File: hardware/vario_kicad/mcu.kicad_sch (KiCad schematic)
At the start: 22 parts, among them U5 STM32L072CBTx, Y1 Crystal, Y2 Crystal_GND24

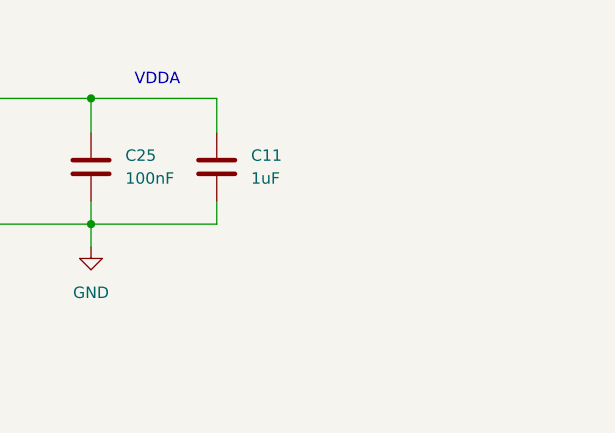
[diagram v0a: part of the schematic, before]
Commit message: add decoupling capacitor for vdd_usb
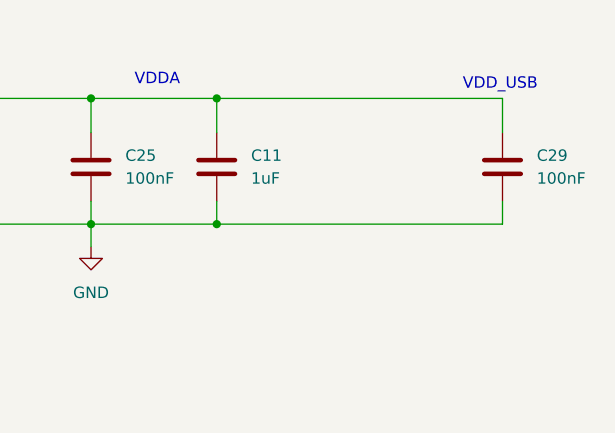
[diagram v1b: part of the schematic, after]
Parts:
- added C29: 100nF, Capacitor_SMD:C_0603_1608Metric, symbol Device:C
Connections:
- net GND: now also C29.2
- net VCC: now also C29.1
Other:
- note added: "VDD_USB"
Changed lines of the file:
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@@
 	(paper "A3")
 	(junction
+		(at 311.15 93.98)
+		(diameter 0)
+		(color 0 0 0 0)
+	)
+	(junction
 		(at 162.56 93.98)
 		(diameter 0)
@@
 	)
 	(junction
+		(at 311.15 107.95)
+		(diameter 0)
+		(color 0 0 0 0)
+	)
+	(junction
 		(at 240.03 107.95)
 		(diameter 0)
@@
 	(wire
 		(pts
+			(xy 311.15 107.95) (xy 342.9 107.95)
+		)
+		(stroke
+			(width 0)
+			(type default)
+		)
+	)
+	(wire
+		(pts
 			(xy 45.72 214.63) (xy 45.72 218.44)
 		)
@@
 	(wire
 		(pts
+			(xy 342.9 93.98) (xy 342.9 97.79)
+		)
+		(stroke
+			(width 0)
+			(type default)
+		)
+	)
+	(wire
+		(pts
 			(xy 123.19 101.6) (xy 123.19 104.14)
 		)
@@
 	(wire
 		(pts
+			(xy 342.9 107.95) (xy 342.9 105.41)
+		)
+		(stroke
+			(width 0)
+			(type default)
+		)
+	)
+	(wire
+		(pts
 			(xy 77.47 153.67) (xy 77.47 156.21)
 		)
@@
 		)
 	)
+	(wire
+		(pts
+			(xy 311.15 93.98) (xy 342.9 93.98)
+		)
+		(stroke
+			(width 0)
+			(type default)
+		)
+	)
 	(rectangle
 		(start 41.91 139.192)
@@
 		)
 	)
+	(text "VDD_USB"
+		(exclude_from_sim no)
+		(at 342.646 92.456 0)
+		(effects
+			(font
+				(size 1.27 1.27)
+			)
+		)
+	)
 	(text "LSE"
 		(exclude_from_sim no)
@@
 					(unit 1)
 				)
+			)
+		)
+	)
+	(symbol
+		(lib_id "Device:C")
+		(at 342.9 101.6 0)
+		(unit 1)
+		(exclude_from_sim no)
+		(in_bom yes)
+		(on_board yes)
+		(dnp no)
+		(fields_autoplaced yes)
+		(property "Reference" "C29"
+			(at 346.71 100.3299 0)
+			(effects
+				(font
+					(size 1.27 1.27)
+				)
+				(justify left)
+			)
+		)
+		(property "Value" "100nF"
+			(at 346.71 102.8699 0)
+			(effects
+				(font
+					(size 1.27 1.27)
+				)
+				(justify left)
+			)
+		)
+		(property "Footprint" "Capacitor_SMD:C_0603_1608Metric"
+			(at 343.8652 105.41 0)
+			(effects
+				(font
+					(size 1.27 1.27)
+				)
+				(hide yes)
+			)
+		)
+		(property "Datasheet" "~"
+			(at 342.9 101.6 0)
+			(effects
+				(font
+					(size 1.27 1.27)
+				)
+				(hide yes)
+			)
+		)
+		(property "Description" "Unpolarized capacitor"
+			(at 342.9 101.6 0)
+			(effects
+				(font
+					(size 1.27 1.27)
+				)
+				(hide yes)
+			)
+		)
+		(property "Sim.Pins" ""
+			(at 342.9 101.6 0)
+			(effects
+				(font
+					(size 1.27 1.27)
+				)
+				(hide yes)
+			)
+		)
+		(pin "2"
+		)
+		(pin "1"
+		)
+		(instances
+			(project "vario_kicad"
+				(path "/50389aff-b244-451e-8e3a-c5addd2215e1/dd2cba4c-5ed6-4588-88fb-827c05b79647"
+					(reference "C29")
+					(unit 1)
+				)

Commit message: add missing footprints
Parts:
- R30: footprint (none) -> Resistor_SMD:R_0402_1005Metric
- TP4: footprint (none) -> TestPoint:TestPoint_Pad_D1.0mm
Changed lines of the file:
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@@
 			)
 		)
-		(property "Footprint" ""
+		(property "Footprint" "Resistor_SMD:R_0402_1005Metric"
 			(at 109.22 230.378 90)
 			(effects
@@
 			)
 		)
-		(property "Footprint" ""
+		(property "Footprint" "TestPoint:TestPoint_Pad_D1.0mm"
 			(at 90.17 121.92 0)
 			(effects

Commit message: layout close to done
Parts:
- removed TP11, TP12: TestPoint, TestPoint:TestPoint_Pad_D1.0mm, symbol Connector:TestPoint
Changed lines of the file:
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@@
-	)
-	(junction
-		(at 203.2 134.62)
-		(diameter 0)
-		(color 0 0 0 0)
 	)
 	(junction
@@
 	)
 	(junction
-		(at 203.2 132.08)
-		(diameter 0)
-		(color 0 0 0 0)
-	)
-	(junction
 		(at 252.73 93.98)
 		(diameter 0)
@@
 	(wire
 		(pts
-			(xy 175.26 134.62) (xy 203.2 134.62)
-		)
-		(stroke
-			(width 0)
-			(type default)
-		)
-	)
-	(wire
-		(pts
 			(xy 128.27 134.62) (xy 139.7 134.62)
 		)
@@
 	(wire
 		(pts
-			(xy 203.2 134.62) (xy 207.01 134.62)
+			(xy 175.26 134.62) (xy 207.01 134.62)
 		)
 		(stroke
@@
 	(wire
 		(pts
-			(xy 203.2 132.08) (xy 207.01 132.08)
+			(xy 175.26 132.08) (xy 207.01 132.08)
 		)
 		(stroke
@@
 		(pts
 			(xy 265.43 93.98) (xy 297.18 93.98)
-		)
-		(stroke
-			(width 0)
-			(type default)
-		)
-	)
-	(wire
-		(pts
-			(xy 175.26 132.08) (xy 203.2 132.08)
 		)
 		(stroke
@@
 	)
 	(symbol
-		(lib_id "Connector:TestPoint")
-		(at 203.2 134.62 180)
-		(unit 1)
-		(exclude_from_sim no)
-		(in_bom yes)
-		(on_board yes)
-		(dnp no)
-		(property "Reference" "TP12"
-			(at 204.216 138.684 0)
-			(effects
-				(font
-					(size 1.27 1.27)
-				)
-				(justify right)
-			)
-		)
-		(property "Value" "TestPoint"
-			(at 205.74 139.1919 0)
-			(effects
-				(font
-					(size 1.27 1.27)
-				)
-				(justify right)
-				(hide yes)
-			)
-		)
-		(property "Footprint" "TestPoint:TestPoint_Pad_D1.0mm"
-			(at 198.12 134.62 0)
-			(effects
-				(font
-					(size 1.27 1.27)
-				)
-				(hide yes)
-			)
-		)
-		(property "Datasheet" "~"
-			(at 198.12 134.62 0)
-			(effects
-				(font
-					(size 1.27 1.27)
-				)
-				(hide yes)
-			)
-		)
-		(property "Description" "test point"
-			(at 203.2 134.62 0)
-			(effects
-				(font
-					(size 1.27 1.27)
-				)
-				(hide yes)
-			)
-		)
-		(property "Sim.Pins" ""
-			(at 203.2 134.62 0)
-			(effects
-				(font
-					(size 1.27 1.27)
-				)
-				(hide yes)
-			)
-		)
-		(pin "1"
-		)
-		(instances
-			(project "vario_kicad"
-				(path "/50389aff-b244-451e-8e3a-c5addd2215e1/dd2cba4c-5ed6-4588-88fb-827c05b79647"
-					(reference "TP12")
-					(unit 1)
-				)
-			)
-		)
-	)
-	(symbol
 		(lib_id "MCU_ST_STM32L0:STM32L072CBTx")
 		(at 157.48 137.16 0)
@@
 					(unit 1)
 				)
-			)
-		)
-	)
-	(symbol
-		(lib_id "Connector:TestPoint")
-		(at 203.2 132.08 0)
-		(unit 1)
-		(exclude_from_sim no)
-		(in_bom yes)
-		(on_board yes)
-		(dnp no)
-		(property "Reference" "TP11"
-			(at 203.962 127.762 0)
-			(effects
-				(font
-					(size 1.27 1.27)
-				)
-				(justify left)
-			)
-		)
-		(property "Value" "TestPoint"
-			(at 205.74 130.0479 0)
-			(effects
-				(font
-					(size 1.27 1.27)
-				)
-				(justify left)
-				(hide yes)
-			)
-		)
-		(property "Footprint" "TestPoint:TestPoint_Pad_D1.0mm"
-			(at 208.28 132.08 0)
-			(effects
-				(font
-					(size 1.27 1.27)
-				)
-				(hide yes)
-			)
-		)
-		(property "Datasheet" "~"
-			(at 208.28 132.08 0)
-			(effects
-				(font
-					(size 1.27 1.27)
-				)
-				(hide yes)
-			)
-		)
-		(property "Description" "test point"
-			(at 203.2 132.08 0)
-			(effects
-				(font
-					(size 1.27 1.27)
-				)
-				(hide yes)
-			)
-		)
-		(property "Sim.Pins" ""
-			(at 203.2 132.08 0)
-			(effects
-				(font
-					(size 1.27 1.27)
-				)
-				(hide yes)
-			)
-		)
-		(pin "1"
-		)
-		(instances
-			(project "vario_kicad"
-				(path "/50389aff-b244-451e-8e3a-c5addd2215e1/dd2cba4c-5ed6-4588-88fb-827c05b79647"
-					(reference "TP11")
-					(unit 1)
-				)

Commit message: remove unnecessary jumper
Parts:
- removed JP1: SolderJumper_2_Bridged, Jumper:SolderJumper-2_P1.3mm_Open_TrianglePad1.0x1.5mm, symbol Jumper:SolderJumper_2_Bridged
- R30: now fitted
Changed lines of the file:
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@@
-	)
-	(junction
-		(at 97.79 218.44)
-		(diameter 0)
-		(color 0 0 0 0)
 	)
 	(junction
@@
 	)
 	(junction
-		(at 120.65 218.44)
-		(diameter 0)
-		(color 0 0 0 0)
-	)
-	(junction
 		(at 157.48 93.98)
 		(diameter 0)
@@
 	(wire
 		(pts
-			(xy 113.03 208.28) (xy 120.65 208.28)
-		)
-		(stroke
-			(width 0)
-			(type default)
-		)
-	)
-	(wire
-		(pts
 			(xy 58.42 171.45) (xy 68.58 171.45)
 		)
@@
 	(wire
 		(pts
-			(xy 120.65 208.28) (xy 120.65 218.44)
-		)
-		(stroke
-			(width 0)
-			(type default)
-		)
-	)
-	(wire
-		(pts
 			(xy 64.77 218.44) (xy 45.72 218.44)
 		)
@@
 	(wire
 		(pts
-			(xy 97.79 218.44) (xy 97.79 208.28)
-		)
-		(stroke
-			(width 0)
-			(type default)
-		)
-	)
-	(wire
-		(pts
 			(xy 240.03 105.41) (xy 240.03 107.95)
 		)
@@
 	(wire
 		(pts
-			(xy 120.65 218.44) (xy 120.65 228.6)
-		)
-		(stroke
-			(width 0)
-			(type default)
-		)
-	)
-	(wire
-		(pts
 			(xy 297.18 93.98) (xy 311.15 93.98)
 		)
@@
 	(wire
 		(pts
-			(xy 97.79 208.28) (xy 105.41 208.28)
-		)
-		(stroke
-			(width 0)
-			(type default)
-		)
-	)
-	(wire
-		(pts
 			(xy 175.26 104.14) (xy 182.88 104.14)
 		)
@@
 	(wire
 		(pts
-			(xy 97.79 228.6) (xy 105.41 228.6)
-		)
-		(stroke
-			(width 0)
-			(type default)
-		)
-	)
-	(wire
-		(pts
 			(xy 76.2 109.22) (xy 113.03 109.22)
 		)
@@
 	(wire
 		(pts
-			(xy 86.36 218.44) (xy 97.79 218.44)
+			(xy 86.36 218.44) (xy 96.52 218.44)
 		)
 		(stroke
@@
 	(wire
 		(pts
-			(xy 120.65 218.44) (xy 132.08 218.44)
+			(xy 104.14 218.44) (xy 116.84 218.44)
 		)
 		(stroke
@@
 		(pts
 			(xy 157.48 179.07) (xy 154.94 179.07)
-		)
-		(stroke
-			(width 0)
-			(type default)
-		)
-	)
-	(wire
-		(pts
-			(xy 97.79 218.44) (xy 97.79 228.6)
-		)
-		(stroke
-			(width 0)
-			(type default)
-		)
-	)
-	(wire
-		(pts
-			(xy 120.65 228.6) (xy 113.03 228.6)
 		)
 		(stroke
@@
 	(rectangle
 		(start 35.306 197.866)
-		(end 147.828 251.46)
+		(end 130.81 251.46)
 		(stroke
 			(width 0)
@@
 	)
 	(label "OSC_OUT"
-		(at 132.08 218.44 0)
+		(at 116.84 218.44 0)
 		(effects
 			(font
@@
 	(symbol
 		(lib_id "Device:R")
-		(at 109.22 228.6 90)
+		(at 100.33 218.44 90)
 		(unit 1)
 		(exclude_from_sim no)
 		(in_bom yes)
 		(on_board yes)
-		(dnp yes)
+		(dnp no)
 		(fields_autoplaced yes)
 		(property "Reference" "R30"
-			(at 109.22 222.25 90)
+			(at 100.33 212.09 90)
 			(effects
 				(font
@@
 		)
 		(property "Value" "0R"
-			(at 109.22 224.79 90)
+			(at 100.33 214.63 90)
 			(effects
 				(font
@@
 		)
 		(property "Footprint" "Resistor_SMD:R_0402_1005Metric"
-			(at 109.22 230.378 90)
+			(at 100.33 220.218 90)
 			(effects
 				(font
@@
 		)
 		(property "Datasheet" "~"
-			(at 109.22 228.6 0)
+			(at 100.33 218.44 0)
 			(effects
 				(font
@@
 		)
 		(property "Description" "Resistor"
-			(at 109.22 228.6 0)
+			(at 100.33 218.44 0)
 			(effects
 				(font
@@
 					(unit 1)
 				)
-			)
-		)
-	)
-	(symbol
-		(lib_id "Jumper:SolderJumper_2_Bridged")
-		(at 109.22 208.28 0)
-		(unit 1)
-		(exclude_from_sim yes)
-		(in_bom no)
-		(on_board yes)
-		(dnp no)
-		(fields_autoplaced yes)
-		(property "Reference" "JP1"
-			(at 109.22 201.93 0)
-			(effects
-				(font
-					(size 1.27 1.27)
-				)
-			)
-		)
-		(property "Value" "SolderJumper_2_Bridged"
-			(at 109.22 204.47 0)
-			(effects
-				(font
-					(size 1.27 1.27)
-				)
-			)
-		)
-		(property "Footprint" "Jumper:SolderJumper-2_P1.3mm_Open_TrianglePad1.0x1.5mm"
-			(at 109.22 208.28 0)
-			(effects
-				(font
-					(size 1.27 1.27)
-				)
-				(hide yes)
-			)
-		)
-		(property "Datasheet" "~"
-			(at 109.22 208.28 0)
-			(effects
-				(font
-					(size 1.27 1.27)
-				)
-				(hide yes)
-			)
-		)
-		(property "Description" "Solder Jumper, 2-pole, closed/bridged"
-			(at 109.22 208.28 0)
-			(effects
-				(font
-					(size 1.27 1.27)
-				)
-				(hide yes)
-			)
-		)
-		(pin "1"
-		)
-		(pin "2"
-		)
-		(instances
-			(project ""
-				(path "/50389aff-b244-451e-8e3a-c5addd2215e1/dd2cba4c-5ed6-4588-88fb-827c05b79647"
-					(reference "JP1")
-					(unit 1)
-				)

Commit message: use 0402 instead of 0603 for almost all caps
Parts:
- C11, C12, C21, C22, C23, C24, C25, C29: footprint Capacitor_SMD:C_0603_1608Metric -> Capacitor_SMD:C_0402_1005Metric
- C4: footprint Capacitor_SMD:C_0603_1608Metric -> Capacitor_SMD:C_0603_1608Metric_Pad1.08x0.95mm_HandSolder
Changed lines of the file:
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@@
 			)
 		)
-		(property "Footprint" "Capacitor_SMD:C_0603_1608Metric"
+		(property "Footprint" "Capacitor_SMD:C_0402_1005Metric"
 			(at 298.1452 105.41 0)
 			(effects
@@
 			)
 		)
-		(property "Footprint" "Capacitor_SMD:C_0603_1608Metric"
+		(property "Footprint" "Capacitor_SMD:C_0402_1005Metric"
 			(at 77.1652 120.65 0)
 			(effects
@@
 			)
 		)
-		(property "Footprint" "Capacitor_SMD:C_0603_1608Metric"
+		(property "Footprint" "Capacitor_SMD:C_0402_1005Metric"
 			(at 266.3952 105.41 0)
 			(effects
@@
 			)
 		)
-		(property "Footprint" "Capacitor_SMD:C_0603_1608Metric"
+		(property "Footprint" "Capacitor_SMD:C_0603_1608Metric_Pad1.08x0.95mm_HandSolder"
 			(at 220.6752 105.41 0)
 			(effects
@@
 			)
 		)
-		(property "Footprint" "Capacitor_SMD:C_0603_1608Metric"
+		(property "Footprint" "Capacitor_SMD:C_0402_1005Metric"
 			(at 45.4152 114.3 0)
 			(effects
@@
 			)
 		)
-		(property "Footprint" "Capacitor_SMD:C_0603_1608Metric"
+		(property "Footprint" "Capacitor_SMD:C_0402_1005Metric"
 			(at 253.6952 105.41 0)
 			(effects
@@
 			)
 		)
-		(property "Footprint" "Capacitor_SMD:C_0603_1608Metric"
+		(property "Footprint" "Capacitor_SMD:C_0402_1005Metric"
 			(at 240.9952 105.41 0)
 			(effects
@@
 			)
 		)
-		(property "Footprint" "Capacitor_SMD:C_0603_1608Metric"
+		(property "Footprint" "Capacitor_SMD:C_0402_1005Metric"
 			(at 312.1152 105.41 0)
 			(effects
@@
 			)
 		)
-		(property "Footprint" "Capacitor_SMD:C_0603_1608Metric"
+		(property "Footprint" "Capacitor_SMD:C_0402_1005Metric"
 			(at 343.8652 105.41 0)
 			(effects

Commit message: layout close to finished
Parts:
- Y2: footprint Crystal:Crystal_SMD_3225-4Pin_3.2x2.5mm_HandSoldering -> Crystal:Crystal_SMD_3225-4Pin_3.2x2.5mm
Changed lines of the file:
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@@
 			)
 		)
-		(property "Footprint" "Crystal:Crystal_SMD_3225-4Pin_3.2x2.5mm_HandSoldering"
+		(property "Footprint" "Crystal:Crystal_SMD_3225-4Pin_3.2x2.5mm"
 			(at 68.58 218.44 0)
 			(effects

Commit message: layout&routing close to done
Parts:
- added C30: 100nF, Capacitor_SMD:C_0402_1005Metric, symbol Device:C
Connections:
- net ADC_IN3: now also C30.1
- net GND: now also C30.2
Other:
- note added: "noise decoupling cap"
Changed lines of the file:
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@@
+	)
+	(junction
+		(at 234.95 115.57)
+		(diameter 0)
+		(color 0 0 0 0)
 	)
 	(junction
@@
 	(wire
 		(pts
-			(xy 175.26 111.76) (xy 182.88 111.76)
+			(xy 234.95 115.57) (xy 243.84 115.57)
 		)
 		(stroke
@@
 	(wire
 		(pts
+			(xy 234.95 115.57) (xy 234.95 111.76)
+		)
+		(stroke
+			(width 0)
+			(type default)
+		)
+	)
+	(wire
+		(pts
 			(xy 113.03 109.22) (xy 139.7 109.22)
 		)
@@
 	(wire
 		(pts
+			(xy 234.95 111.76) (xy 175.26 111.76)
+		)
+		(stroke
+			(width 0)
+			(type default)
+		)
+	)
+	(wire
+		(pts
 			(xy 157.48 179.07) (xy 157.48 181.61)
 		)
@@
 	(wire
 		(pts
+			(xy 234.95 127) (xy 234.95 130.81)
+		)
+		(stroke
+			(width 0)
+			(type default)
+		)
+	)
+	(wire
+		(pts
 			(xy 45.72 237.49) (xy 68.58 237.49)
 		)
@@
 		(pts
 			(xy 311.15 93.98) (xy 342.9 93.98)
+		)
+		(stroke
+			(width 0)
+			(type default)
+		)
+	)
+	(wire
+		(pts
+			(xy 234.95 115.57) (xy 234.95 119.38)
 		)
 		(stroke
@@
 		)
 	)
+	(text "noise decoupling cap\n"
+		(exclude_from_sim no)
+		(at 243.078 127.762 0)
+		(effects
+			(font
+				(size 0.762 0.762)
+			)
+		)
+	)
 	(text "MCU"
 		(exclude_from_sim no)
@@
 	(hierarchical_label "ADC_IN3"
 		(shape input)
-		(at 182.88 111.76 0)
+		(at 243.84 115.57 0)
 		(effects
 			(font
@@
 	)
 	(symbol
+		(lib_id "power:GND")
+		(at 234.95 130.81 0)
+		(unit 1)
+		(exclude_from_sim no)
+		(in_bom yes)
+		(on_board yes)
+		(dnp no)
+		(fields_autoplaced yes)
+		(property "Reference" "#PWR39"
+			(at 234.95 137.16 0)
+			(effects
+				(font
+					(size 1.27 1.27)
+				)
+				(hide yes)
+			)
+		)
+		(property "Value" "GND"
+			(at 234.95 135.89 0)
+			(effects
+				(font
+					(size 1.27 1.27)
+				)
+			)
+		)
+		(property "Footprint" ""
+			(at 234.95 130.81 0)
+			(effects
+				(font
+					(size 1.27 1.27)
+				)
+				(hide yes)
+			)
+		)
+		(property "Datasheet" ""
+			(at 234.95 130.81 0)
+			(effects
+				(font
+					(size 1.27 1.27)
+				)
+				(hide yes)
+			)
+		)
+		(property "Description" "Power symbol creates a global label with name \"GND\" , ground"
+			(at 234.95 130.81 0)
+			(effects
+				(font
+					(size 1.27 1.27)
+				)
+				(hide yes)
+			)
+		)
+		(pin "1"
+		)
+		(instances
+			(project ""
+				(path "/50389aff-b244-451e-8e3a-c5addd2215e1/dd2cba4c-5ed6-4588-88fb-827c05b79647"
+					(reference "#PWR39")
+					(unit 1)
+				)
+			)
+		)
+	)
+	(symbol
 		(lib_id "Device:C")
 		(at 76.2 116.84 0)
@@
 					(unit 1)
 				)
+			)
+		)
+	)
+	(symbol
+		(lib_id "Device:C")
+		(at 234.95 123.19 0)
+		(unit 1)
+		(exclude_from_sim no)
+		(in_bom yes)
+		(on_board yes)
+		(dnp no)
+		(property "Reference" "C30"
+			(at 238.76 121.9199 0)
+			(effects
+				(font
+					(size 1.27 1.27)
+				)
+				(justify left)
+			)
+		)
+		(property "Value" "100nF"
+			(at 238.76 124.4599 0)
+			(effects
+				(font
+					(size 1.27 1.27)
+				)
+				(justify left)
+			)
+		)
+		(property "Footprint" "Capacitor_SMD:C_0402_1005Metric"
+			(at 235.9152 127 0)
+			(effects
+				(font
+					(size 1.27 1.27)
+				)
+				(hide yes)
+			)
+		)
+		(property "Datasheet" "~"
+			(at 234.95 123.19 0)
+			(effects
+				(font
+					(size 1.27 1.27)
+				)
+				(hide yes)
+			)
+		)
+		(property "Description" "Unpolarized capacitor"
+			(at 234.95 123.19 0)
+			(effects
+				(font
+					(size 1.27 1.27)
+				)
+				(hide yes)
+			)
+		)
+		(property "Sim.Pins" ""
+			(at 234.95 123.19 0)
+			(effects
+				(font
+					(size 1.27 1.27)
+				)
+				(hide yes)
+			)
+		)
+		(pin "2"
+		)
+		(pin "1"
+		)
+		(instances
+			(project "vario_kicad"
+				(path "/50389aff-b244-451e-8e3a-c5addd2215e1/dd2cba4c-5ed6-4588-88fb-827c05b79647"
+					(reference "C30")
+					(unit 1)
+				)

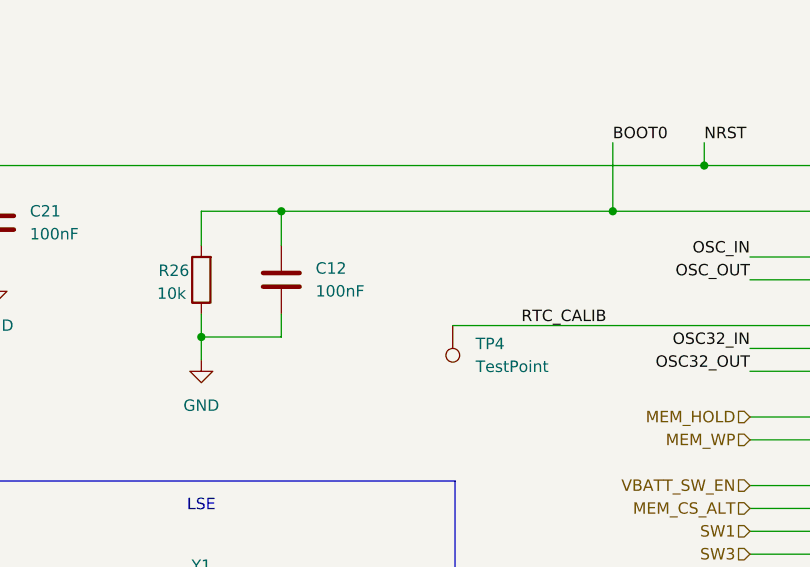
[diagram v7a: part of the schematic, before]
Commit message: remove capacitor to boot0 pin
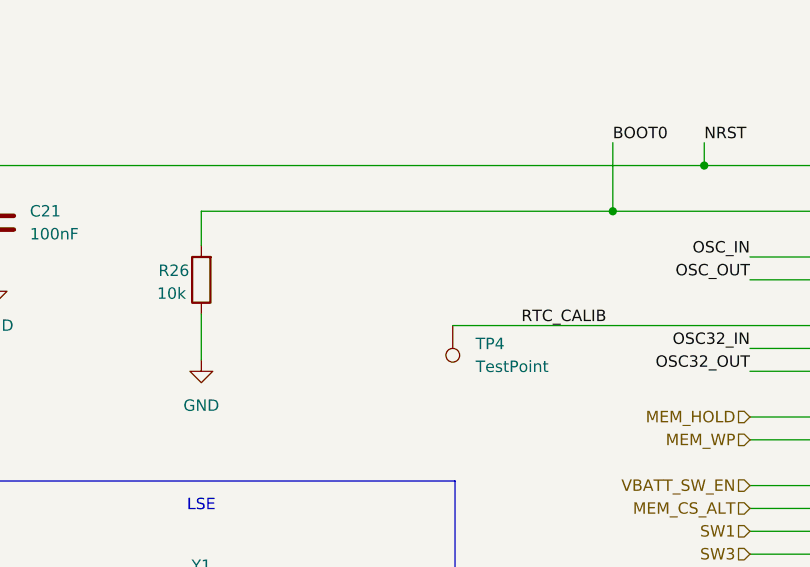
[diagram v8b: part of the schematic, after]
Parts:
- removed C12: 100nF, Capacitor_SMD:C_0402_1005Metric, symbol Device:C
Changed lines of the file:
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@@
-	)
-	(junction
-		(at 67.31 123.19)
-		(diameter 0)
-		(color 0 0 0 0)
 	)
 	(junction
@@
 		(color 0 0 0 0)
 	)
-	(junction
-		(at 76.2 109.22)
-		(diameter 0)
-		(color 0 0 0 0)
-	)
 	(no_connect
 		(at 139.7 157.48)
@@
 	(wire
 		(pts
-			(xy 76.2 120.65) (xy 76.2 123.19)
-		)
-		(stroke
-			(width 0)
-			(type default)
-		)
-	)
-	(wire
-		(pts
 			(xy 311.15 105.41) (xy 311.15 107.95)
 		)
@@
 	(wire
 		(pts
-			(xy 67.31 120.65) (xy 67.31 123.19)
-		)
-		(stroke
-			(width 0)
-			(type default)
-		)
-	)
-	(wire
-		(pts
 			(xy 58.42 156.21) (xy 58.42 160.02)
 		)
@@
 	(wire
 		(pts
-			(xy 67.31 109.22) (xy 76.2 109.22)
+			(xy 67.31 109.22) (xy 113.03 109.22)
 		)
 		(stroke
@@
 	(wire
 		(pts
-			(xy 76.2 109.22) (xy 113.03 109.22)
-		)
-		(stroke
-			(width 0)
-			(type default)
-		)
-	)
-	(wire
-		(pts
 			(xy 154.94 93.98) (xy 157.48 93.98)
 		)
@@
 	(wire
 		(pts
-			(xy 76.2 123.19) (xy 67.31 123.19)
-		)
-		(stroke
-			(width 0)
-			(type default)
-		)
-	)
-	(wire
-		(pts
 			(xy 68.58 237.49) (xy 68.58 243.84)
 		)
@@
 	(wire
 		(pts
-			(xy 67.31 123.19) (xy 67.31 125.73)
+			(xy 67.31 120.65) (xy 67.31 125.73)
 		)
 		(stroke
@@
 		(pts
 			(xy 86.36 232.41) (xy 86.36 237.49)
-		)
-		(stroke
-			(width 0)
-			(type default)
-		)
-	)
-	(wire
-		(pts
-			(xy 76.2 109.22) (xy 76.2 113.03)
 		)
 		(stroke
@@
 					(unit 1)
 				)
-			)
-		)
-	)
-	(symbol
-		(lib_id "Device:C")
-		(at 76.2 116.84 0)
-		(unit 1)
-		(exclude_from_sim no)
-		(in_bom yes)
-		(on_board yes)
-		(dnp no)
-		(fields_autoplaced yes)
-		(property "Reference" "C12"
-			(at 80.01 115.5699 0)
-			(effects
-				(font
-					(size 1.27 1.27)
-				)
-				(justify left)
-			)
-		)
-		(property "Value" "100nF"
-			(at 80.01 118.1099 0)
-			(effects
-				(font
-					(size 1.27 1.27)
-				)
-				(justify left)
-			)
-		)
-		(property "Footprint" "Capacitor_SMD:C_0402_1005Metric"
-			(at 77.1652 120.65 0)
-			(effects
-				(font
-					(size 1.27 1.27)
-				)
-				(hide yes)
-			)
-		)
-		(property "Datasheet" "~"
-			(at 76.2 116.84 0)
-			(effects
-				(font
-					(size 1.27 1.27)
-				)
-				(hide yes)
-			)
-		)
-		(property "Description" "Unpolarized capacitor"
-			(at 76.2 116.84 0)
-			(effects
-				(font
-					(size 1.27 1.27)
-				)
-				(hide yes)
-			)
-		)
-		(property "Sim.Pins" ""
-			(at 76.2 116.84 0)
-			(effects
-				(font
-					(size 1.27 1.27)
-				)
-				(hide yes)
-			)
-		)
-		(pin "2"
-		)
-		(pin "1"
-		)
-		(instances
-			(project "vario_kicad"
-				(path "/50389aff-b244-451e-8e3a-c5addd2215e1/dd2cba4c-5ed6-4588-88fb-827c05b79647"
-					(reference "C12")
-					(unit 1)
-				)
